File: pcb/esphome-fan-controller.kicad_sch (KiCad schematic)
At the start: 49 parts, among them J1 Screw_Terminal_01x02, J2 USB-C, M1 Fan_CPU_4pin, U1 MPM3506AGQV-P, U2 TPS61322DBZ, U3 ESP32-C3-MINI-1, U4 SN74LV1T34DBV, U5 SN74LV1T34DBV, U6 LM76202-Q1

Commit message: Update notes on schematic
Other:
- note added: "Notes 1. Input voltage range 5 to 24V. Operating current 2A."
- note removed: "Notes 1. Input voltage range 5 to 24V. Operating current 2A. 2. 3-Pin Fan speed support add jumper, TP1 to U6-7 (~{SHDN} Pin)."
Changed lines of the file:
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@@
 		)
 	)
-	(text "Notes\n1. Input voltage range 5 to 24V. Operating current 2A.\n2. 3-Pin Fan speed support add jumper, TP1 to U6-7 (~{SHDN} Pin).\n"
+	(text "Notes\n1. Input voltage range 5 to 24V. Operating current 2A."
 		(exclude_from_sim no)
 		(at 160.02 153.416 0)

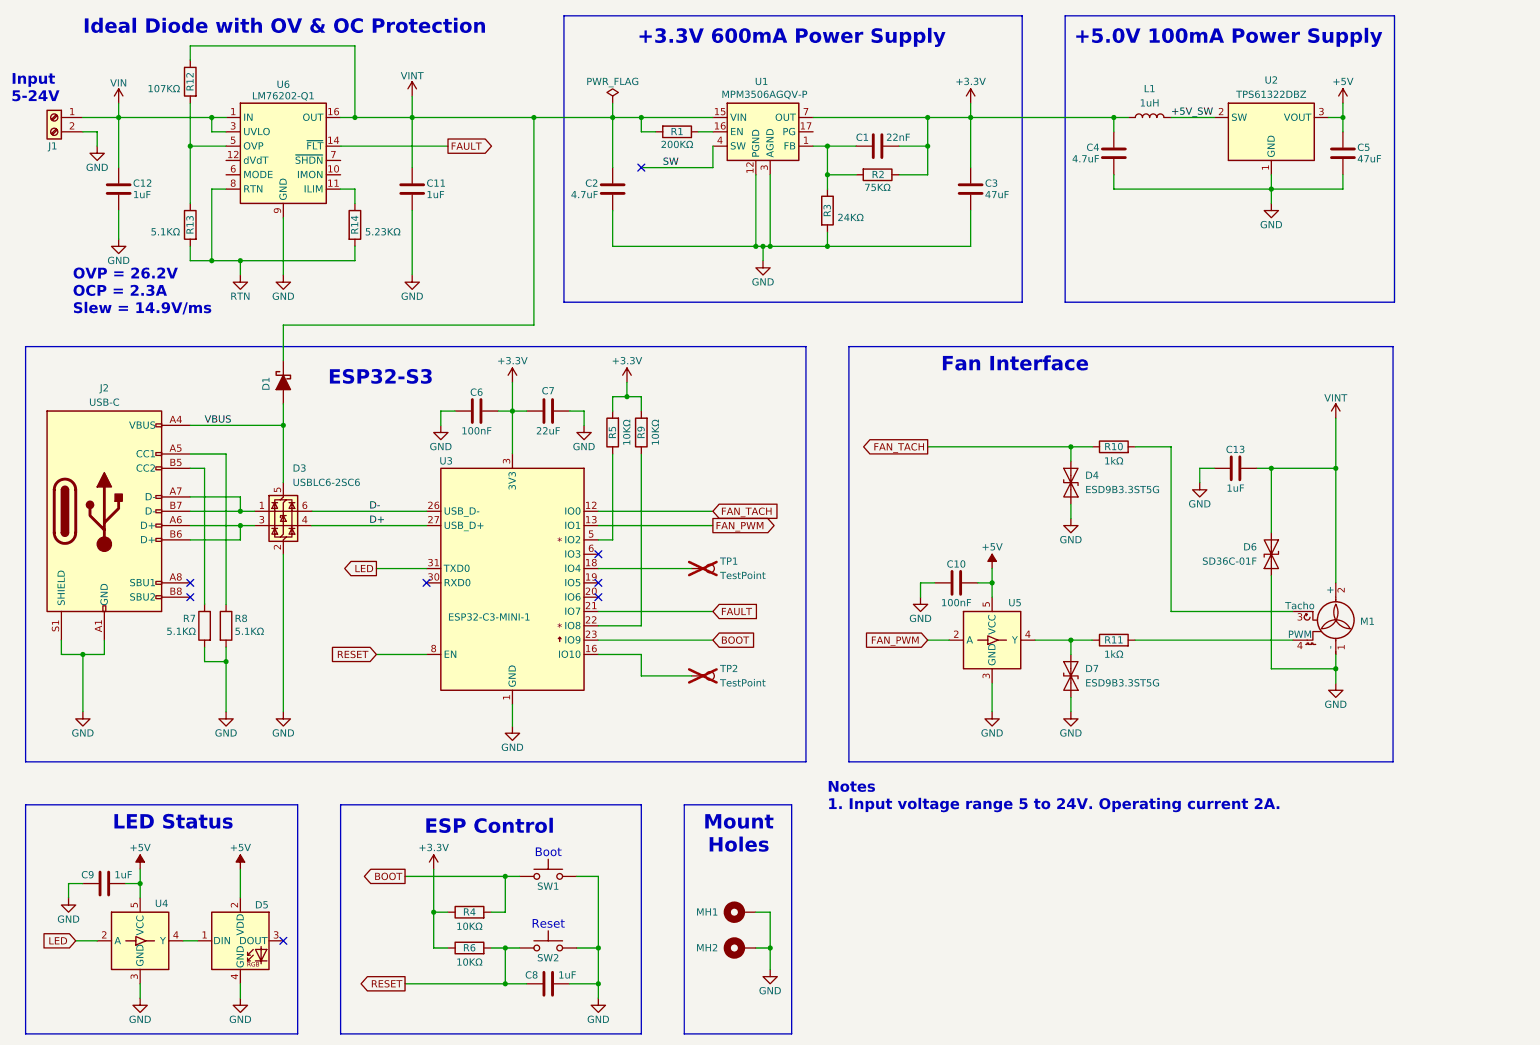
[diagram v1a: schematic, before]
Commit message: Update PCB to Rev A 5V power supply now uses TPS613222A. Different package with correct voltage. Replace fan interface ESD diodes with dual TVS in SOT-23 package. Shutdown on LM76202 can be used to reduce fan power on 3-Pins. Add D4 to support 3-Pin fans. Move all components to top side.
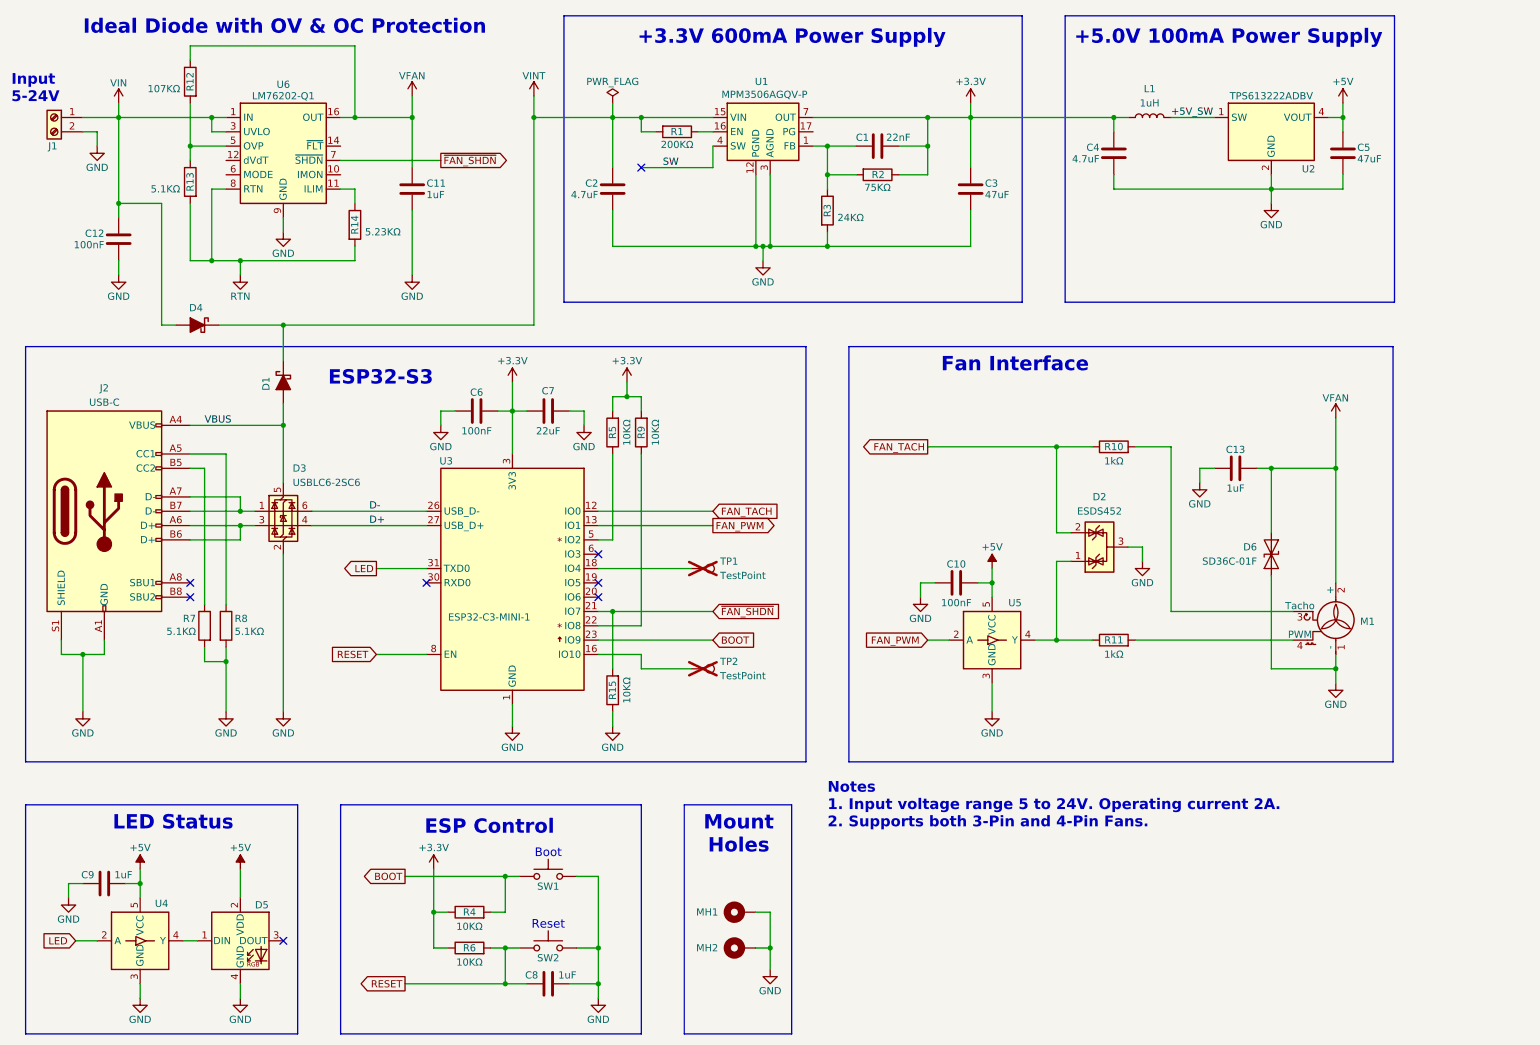
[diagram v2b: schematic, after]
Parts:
- removed D4, D7: ESD9B3.3ST5G, Diode_SMD:D_SOD-923, symbol Diode:ESD9B3.3ST5G
- removed U2: TPS61322DBZ, Package_TO_SOT_SMD:SOT-23, symbol Regulator_Switching:TPS61322DBZ
- added D2: ESDS452, Package_TO_SOT_SMD:SOT-23, symbol Power_Protection:NUP2105L
- added D4: SS2FH6HM3/H, Diode_SMD:D_SMF, symbol Device:D_Schottky_Filled
- added R15: 10KΩ, Resistor_SMD:R_0402_1005Metric, symbol Device:R
- added U2: TPS613222ADBV, Package_TO_SOT_SMD:SOT-23-5, symbol Regulator_Switching:TPS613222ADBV
- C12: value 1uF -> 100nF; footprint Capacitor_SMD:C_0805_2012Metric -> Capacitor_SMD:C_0402_1005Metric; Manufacturer YAGEO -> Samsung; Part Number CC0805MKY5V9BB105 -> CL05B104KB54PNC
- J1: footprint Connector_Phoenix_MC:PhoenixContact_MCV_1,5_2-G-3.81_1x02_P3.81mm_Vertical -> 1984769:1984769; Part Number 1803426 -> 1988956
- R10, R11: footprint Resistor_SMD:R_0805_2012Metric -> Resistor_SMD:R_0402_1005Metric; Part Number CRCW08051K00FKEAC -> CRCW04021K0FKED
- U1: Manufacturer_Name (none) -> Monolithic Power Systems (MPS); Manufacturer_Part_Number (none) -> MPM3506AGQV-P; Mouser Part Number (none) -> 946-MPM3506AGQV-P; Mouser Price/Stock (none) -> https://www.monolithicpower.com/en/documentview/productdocu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
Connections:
- net +5V: now also U2.4 (VOUT)
- net +5V_SW: now also U2.1 (SW)
- net FAN_TACH: now also D2.2 (K)
- net GND: now also D2.3 (A), R15.1, U2.2 (GND)
- net IN_2: now also D4.2 (A)
- net VINT: now also D4.1 (K); no longer C11.1, C13.2, D6.2 (A2), M1.2 (+), R12.1, U6.15 (OUT_2), U6.16 (OUT)
- net ~{FAN_SHDN}: now reaches U6.7 (~{SHDN})
- net ~{FAN_SHDN}: now also U3.21 (IO7), R15.2
- net at R11.1, U5.4 (Y): now also D2.1 (K)
- net FAULT: no longer names the net of U6.14 (~{FLT})
- net FAULT: no longer U3.21 (IO7)
- new net VFAN: C11.1, C13.2, D6.2 (A2), M1.2 (+), R12.1, U6.15 (OUT_2), U6.16 (OUT)
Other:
- note added: "Notes 1. Input voltage range 5 to 24V. Operating current 2A. 2. Supports both 3-Pin and 4-Pin Fans."
- note removed: "Notes 1. Input voltage range 5 to 24V. Operating current 2A."
- note removed: "OVP = 26.2V OCP = 2.3A Slew = 14.9V/ms"
- moved on the sheet: C12, R13, TP2
